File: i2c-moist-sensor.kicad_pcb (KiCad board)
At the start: 2 copper layers, 18 x 149 mm, 24 parts, among them IC1 ATTINY441-SSU, P1 CONN_02X03, X1 16MHz

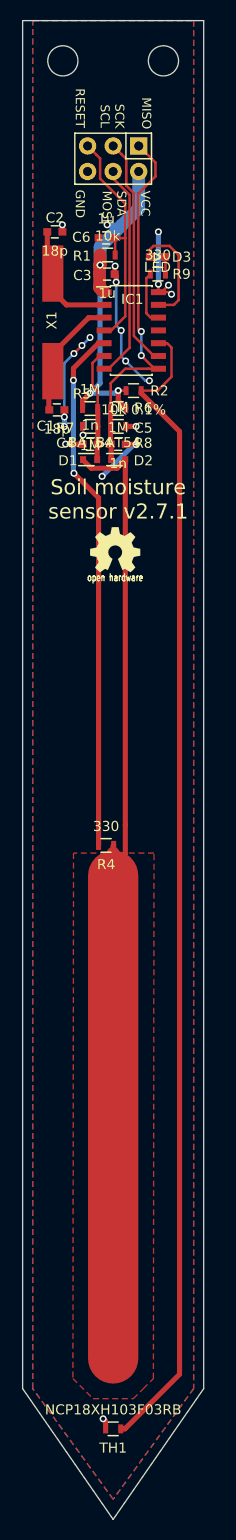
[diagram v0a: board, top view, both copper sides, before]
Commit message: New eeschema libs are new. Move TH1 and R4 OUT of the soil. Minimize stray capacitance where it matters
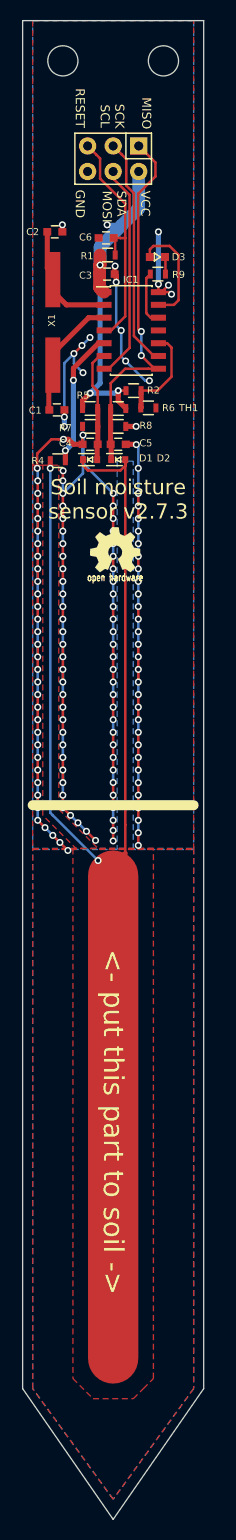
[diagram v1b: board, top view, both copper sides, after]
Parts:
- added G***: LOGO, chirp_logo:ziogas, F.Cu at (95.5, 37.0)
- moved TH1 101.6 mm to (98.5, 51.5), turned to 0 degrees
- moved R4 38.5 mm to (89.5, 56.8), turned to 0 degrees
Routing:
- net GND: track 43.6 -> 223.7 mm, vias 21 -> 144
- net /THERMISTOR: track 115.4 -> 9.70 mm
- net /SENSOR_TRACK: track 98.7 -> 140.8 mm, vias 0 -> 2
- net /EXCITATION: track 52.6 -> 13.6 mm
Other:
- net class excitation added: clearance 0.6, trace_width 0.254, via_dia 0.7, via_drill 0.4
- board text added: "<- put this part to soil ->"
- board text added: "Soil moisture sensor v2.7.3"
- board text removed: "Soil moisture sensor v2.7.1"

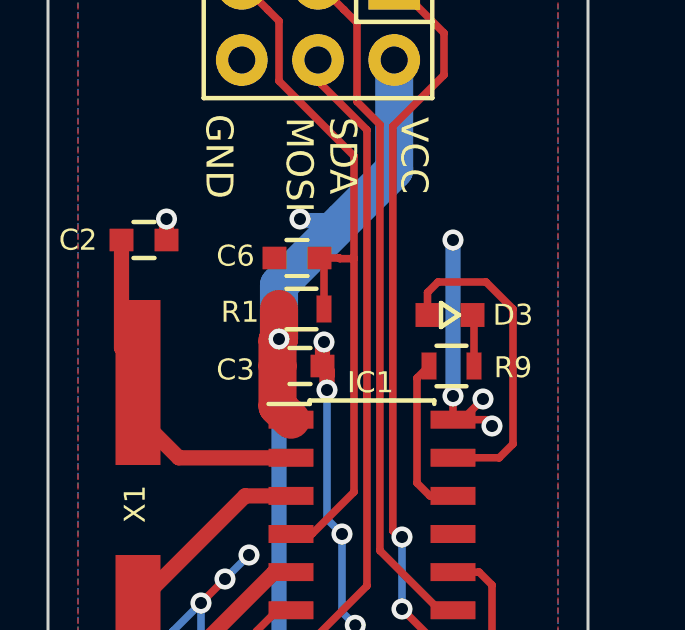
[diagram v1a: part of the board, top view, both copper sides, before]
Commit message: Fix LED footprint according to the datasheet, add data for the bom to schematics
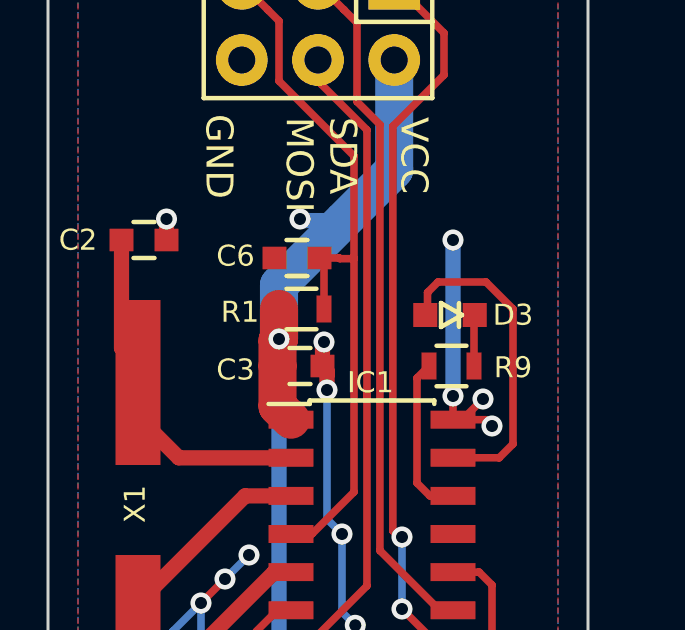
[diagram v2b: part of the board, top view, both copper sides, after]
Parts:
- turned D3 to 270 degrees
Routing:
- net Net-(D3-Pad2): track 1.72 -> 4.57 mm
- net Net-(D3-Pad1): track 10.8 -> 7.96 mm
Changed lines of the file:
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@@
-(kicad_pcb (version 4) (host pcbnew 0.201510221816+6274~30~ubuntu14.04.1-product)
+(kicad_pcb (version 4) (host pcbnew 0.201510241816+6277~30~ubuntu14.04.1-product)
   (general
     (links 42)
-    (no_connects 0)
-    (area 85.949999 12.949999 104.050001 162.050001)
+    (no_connects 2)
+    (area 83.111667 11.7445 114.755001 162.050001)
     (thickness 1.6)
     (drawings 16)
@@
     (pad_drill 0)
     (pad_to_mask_clearance 0)
+    (pad_to_paste_clearance -0.003)
     (aux_axis_origin 0 0)
-    (visible_elements FFFEFF7F)
+    (visible_elements FFFFFF7F)
     (pcbplotparams
       (layerselection 0x010f0_80000001)
@@
     (uvia_drill 0.127)
   )
+  (module LEDs:LED-0603 (layer F.Cu)
+    (at 99.4 36.5 270)
+    (descr "LED 0603 smd package")
+    (tags "LED led 0603 SMD smd SMT smt smdled SMDLED smtled SMTLED")
+    (attr smd)
+    (fp_text reference D3 (at 0 -2.1 360) (layer F.SilkS)
+      (effects (font (size 0.7 0.7) (thickness 0.11)))
+    )
+    (fp_text value LED (at 0 -4.1 360) (layer F.Fab)
+      (effects (font (size 0.7 0.7) (thickness 0.11)))
+    )
+    (fp_line (start 0.4 -0.3) (end -0.4 -0.3) (layer F.SilkS) (width 0.15))
+    (fp_line (start 0.4 0.3) (end 0 -0.4) (layer F.SilkS) (width 0.15))
+    (fp_line (start -0.4 0.3) (end 0.4 0.3) (layer F.SilkS) (width 0.15))
+    (fp_line (start 0 -0.4) (end -0.4 0.3) (layer F.SilkS) (width 0.15))
+    (pad 1 smd rect (at 0 0.825 270) (size 0.8 0.8) (layers F.Cu F.Paste F.Mask)
+      (net 11 "Net-(D3-Pad1)"))
+    (pad 2 smd rect (at 0 -0.825 270) (size 0.8 0.8) (layers F.Cu F.Paste F.Mask)
+      (net 10 "Net-(D3-Pad2)"))
+  )
   (module Crystals:Crystal_HC49-SD_SMD (layer F.Cu)
     (at 89 43 90)
@@
     (pad 2 smd rect (at 0.7 0 180) (size 0.6 0.7) (layers F.Cu F.Paste F.Mask)
       (net 6 /SENSOR_TRACK))
-  )
-  (module LEDs:LED-0603 (layer F.Cu)
-    (at 99.4 36.5)
-    (descr "LED 0603 smd package")
-    (tags "LED led 0603 SMD smd SMT smt smdled SMDLED smtled SMTLED")
-    (attr smd)
-    (fp_text reference D3 (at 2.1 0) (layer F.SilkS)
-      (effects (font (size 0.7 0.7) (thickness 0.11)))
-    )
-    (fp_text value LED (at 4.1 0) (layer F.Fab)
-      (effects (font (size 0.7 0.7) (thickness 0.11)))
-    )
-    (fp_line (start -0.3 -0.4) (end -0.3 0.4) (layer F.SilkS) (width 0.15))
-    (fp_line (start -0.3 0.4) (end 0.3 0) (layer F.SilkS) (width 0.15))
-    (fp_line (start 0.3 0) (end -0.3 -0.4) (layer F.SilkS) (width 0.15))
-    (pad 1 smd rect (at -0.7493 0) (size 0.79756 0.79756) (layers F.Cu F.Paste F.Mask)
-      (net 11 "Net-(D3-Pad1)"))
-    (pad 2 smd rect (at 0.7493 0) (size 0.79756 0.79756) (layers F.Cu F.Paste F.Mask)
-      (net 10 "Net-(D3-Pad2)"))
   )
   (module Pin_Headers:Pin_Header_Straight_2x03 (layer F.Cu)
@@
   (segment (start 100.2 38.2) (end 100.2 36.5507) (width 0.254) (layer F.Cu) (net 10))
   (segment (start 100.2 36.5507) (end 100.1493 36.5) (width 0.254) (layer F.Cu) (net 10))
+  (segment (start 100.6 35.4) (end 99 35.4) (width 0.254) (layer F.Cu) (net 10))
+  (segment (start 99 35.4) (end 98.6507 35.7493) (width 0.254) (layer F.Cu) (net 10))
+  (segment (start 98.6507 35.7493) (end 98.6507 36.5) (width 0.254) (layer F.Cu) (net 10))
   (segment (start 99.5 41.26) (end 101.04 41.26) (width 0.254) (layer F.Cu) (net 11))
   (segment (start 101.04 41.26) (end 101.5 40.8) (width 0.254) (layer F.Cu) (net 11))
   (segment (start 101.5 40.8) (end 101.5 36.3) (width 0.254) (layer F.Cu) (net 11))
   (segment (start 101.5 36.3) (end 100.6 35.4) (width 0.254) (layer F.Cu) (net 11))
-  (segment (start 100.6 35.4) (end 99 35.4) (width 0.254) (layer F.Cu) (net 11))
-  (segment (start 99 35.4) (end 98.6507 35.7493) (width 0.254) (layer F.Cu) (net 11))
-  (segment (start 98.6507 35.7493) (end 98.6507 36.5) (width 0.254) (layer F.Cu) (net 11))
   (segment (start 96.3 29.38933) (end 96.3 26.76) (width 0.254) (layer F.Cu) (net 12))
   (segment (start 97.06362 30.152949) (end 96.3 29.38933) (width 0.254) (layer F.Cu) (net 12))

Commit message: Put the new version to the pannel
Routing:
- net Net-(D3-Pad2): track 4.57 -> 1.72 mm
- net Net-(D3-Pad1): track 7.96 -> 10.8 mm
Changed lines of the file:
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@@
-(kicad_pcb (version 4) (host pcbnew 0.201510241816+6277~30~ubuntu14.04.1-product)
+(kicad_pcb (version 4) (host pcbnew 0.201510251816+6278~30~ubuntu14.04.1-product)
   (general
     (links 42)
-    (no_connects 2)
-    (area 83.111667 11.7445 114.755001 162.050001)
+    (no_connects 0)
+    (area 85.949999 12.949999 104.050001 162.050001)
     (thickness 1.6)
     (drawings 16)
@@
     (visible_elements FFFFFF7F)
     (pcbplotparams
-      (layerselection 0x010f0_80000001)
+      (layerselection 0x010f8_80000001)
       (usegerberextensions false)
       (excludeedgelayer true)
@@
       (effects (font (size 0.7 0.7) (thickness 0.11)))
     )
-    (fp_text value BAT54 (at -5.996 0.142 180) (layer F.Fab)
+    (fp_text value BAT54 (at -7.246 0.142 180) (layer F.Fab)
       (effects (font (size 0.7 0.7) (thickness 0.11)))
     )
@@
       (effects (font (size 0.7 0.7) (thickness 0.11)))
     )
-    (fp_text value BAT54 (at -12.54 0.142 180) (layer F.Fab)
+    (fp_text value BAT54 (at -13.54 0.142 180) (layer F.Fab)
       (effects (font (size 0.7 0.7) (thickness 0.11)))
     )
@@
   (segment (start 100.2 38.2) (end 100.2 36.5507) (width 0.254) (layer F.Cu) (net 10))
   (segment (start 100.2 36.5507) (end 100.1493 36.5) (width 0.254) (layer F.Cu) (net 10))
-  (segment (start 100.6 35.4) (end 99 35.4) (width 0.254) (layer F.Cu) (net 10))
-  (segment (start 99 35.4) (end 98.6507 35.7493) (width 0.254) (layer F.Cu) (net 10))
-  (segment (start 98.6507 35.7493) (end 98.6507 36.5) (width 0.254) (layer F.Cu) (net 10))
+  (segment (start 100.6 35.4) (end 99 35.4) (width 0.254) (layer F.Cu) (net 11))
+  (segment (start 99 35.4) (end 98.6507 35.7493) (width 0.254) (layer F.Cu) (net 11))
+  (segment (start 98.6507 35.7493) (end 98.6507 36.5) (width 0.254) (layer F.Cu) (net 11))
   (segment (start 99.5 41.26) (end 101.04 41.26) (width 0.254) (layer F.Cu) (net 11))
   (segment (start 101.04 41.26) (end 101.5 40.8) (width 0.254) (layer F.Cu) (net 11))

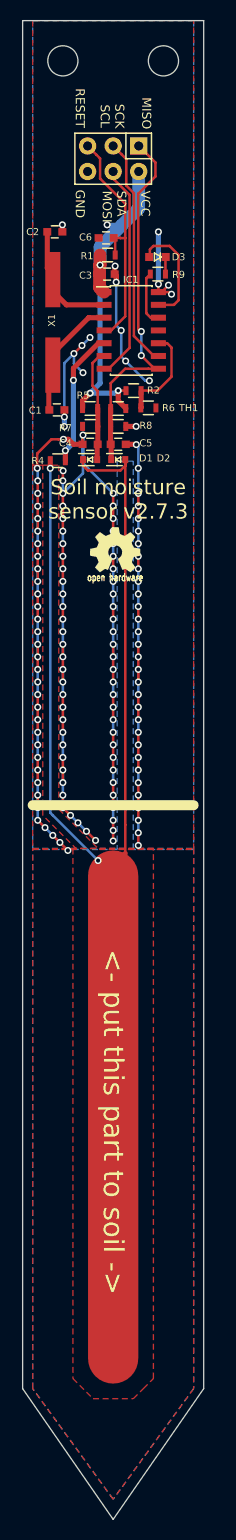
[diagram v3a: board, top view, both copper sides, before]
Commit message: Remove sharp corners so that heatshrink lays nicer
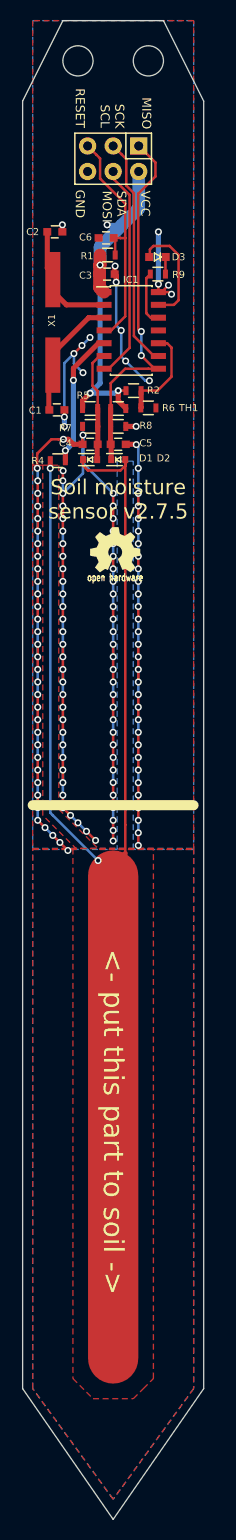
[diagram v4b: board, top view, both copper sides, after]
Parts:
- moved REF** 1.50 mm to (91.5, 17.0)
- moved REF** 1.50 mm to (98.5, 17.0)
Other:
- outline, holes or cut-outs redrawn
- board text added: "Soil moisture sensor v2.7.5"
- board text removed: "Soil moisture sensor v2.7.3"
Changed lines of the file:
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@@
-(kicad_pcb (version 4) (host pcbnew 0.201510251816+6278~30~ubuntu14.04.1-product)
+(kicad_pcb (version 20160815) (host pcbnew no-vcs-found-7518~57~ubuntu14.04.1)
   (general
     (links 42)
@@
     (area 85.949999 12.949999 104.050001 162.050001)
     (thickness 1.6)
-    (drawings 16)
+    (drawings 20)
     (tracks 462)
     (zones 0)
@@
       (hpglpenspeed 20)
       (hpglpendiameter 15)
-      (hpglpenoverlay 2)
       (psnegative false)
       (psa4output false)
@@
     (tags "LED led 0603 SMD smd SMT smt smdled SMDLED smtled SMTLED")
     (attr smd)
-    (fp_text reference D3 (at 0 -2.1 360) (layer F.SilkS)
-      (effects (font (size 0.7 0.7) (thickness 0.11)))
-    )
-    (fp_text value LED (at 0 -4.1 360) (layer F.Fab)
+    (fp_text reference D3 (at 0 -2.1) (layer F.SilkS)
+      (effects (font (size 0.7 0.7) (thickness 0.11)))
+    )
+    (fp_text value LED (at 0 -4.1) (layer F.Fab)
       (effects (font (size 0.7 0.7) (thickness 0.11)))
     )
@@
     (pad 2 smd rect (at 0 -0.825 270) (size 0.8 0.8) (layers F.Cu F.Paste F.Mask)
       (net 10 "Net-(D3-Pad2)"))
+    (model "${KIPRJMOD}/3d/User Library-LTST-C190GKT.STEP"
+      (at (xyz 0 0 0))
+      (scale (xyz 1 1 1))
+      (rotate (xyz 0 0 0))
+    )
   )
   (module Crystals:Crystal_HC49-SD_SMD (layer F.Cu)
@@
     (pad 2 smd rect (at 4.25 0 90) (size 5.5 1.5) (layers F.Cu F.Paste F.Mask)
       (net 3 "Net-(C2-Pad1)"))
-    (model Crystals_Oscillators_SMD/Q_49U3HMS.wrl
+    (model "${KIPRJMOD}/3d/User Library-Crystal HC49_US-SM.STEP"
       (at (xyz 0 0 0))
       (scale (xyz 1 1 1))
@@
     (pad 2 smd rect (at 0.7 0 180) (size 0.6 0.7) (layers F.Cu F.Paste F.Mask)
       (net 14 /MISO/SENSE_HIGH))
+    (model "${KIPRJMOD}/3d/User Library-SOD523-2.STEP"
+      (at (xyz 0 0 0))
+      (scale (xyz 1 1 1))
+      (rotate (xyz -90 0 90))
+    )
   )
   (module SMD_Packages:SOD-523 (layer F.Cu)
@@
     (pad 2 smd rect (at 0.7 0 180) (size 0.6 0.7) (layers F.Cu F.Paste F.Mask)
       (net 6 /SENSOR_TRACK))
+    (model "${KIPRJMOD}/3d/User Library-SOD523-2.STEP"
+      (at (xyz 0 0 0))
+      (scale (xyz 1 1 1))
+      (rotate (xyz -90 0 90))
+    )
   )
   (module Pin_Headers:Pin_Header_Straight_2x03 (layer F.Cu)
@@
     (pad 2 smd rect (at 0.75 0) (size 0.8 0.75) (layers F.Cu F.Paste F.Mask)
       (net 2 GND))
-    (model Capacitors_SMD/C_0603.wrl
+    (model "${KIPRJMOD}/3d/User Library-CAP_SMD-1.STEP"
       (at (xyz 0 0 0))
       (scale (xyz 1 1 1))
@@
     (pad 2 smd rect (at 0.75 0) (size 0.8 0.75) (layers F.Cu F.Paste F.Mask)
       (net 2 GND))
-    (model Capacitors_SMD/C_0603.wrl
+    (model "${KIPRJMOD}/3d/User Library-CAP_SMD-1.STEP"
       (at (xyz 0 0 0))
       (scale (xyz 1 1 1))
@@
     (pad 2 smd rect (at 0.75 0) (size 0.8 0.75) (layers F.Cu F.Paste F.Mask)
       (net 2 GND))
-    (model Capacitors_SMD/C_0603.wrl
+    (model "${KIPRJMOD}/3d/User Library-CAP_SMD-1.STEP"
       (at (xyz 0 0 0))
       (scale (xyz 1 1 1))
@@
     (pad 2 smd rect (at 0.75 0 180) (size 0.8 0.75) (layers F.Cu F.Paste F.Mask)
       (net 2 GND))
-    (model Capacitors_SMD/C_0603.wrl
+    (model "${KIPRJMOD}/3d/User Library-CAP_SMD-1.STEP"
       (at (xyz 0 0 0))
       (scale (xyz 1 1 1))
@@
     (pad 2 smd rect (at 0.75 0) (size 0.8 0.75) (layers F.Cu F.Paste F.Mask)
       (net 2 GND))
-    (model Capacitors_SMD/C_0603.wrl
+    (model "${KIPRJMOD}/3d/User Library-CAP_SMD-1.STEP"
       (at (xyz 0 0 0))
       (scale (xyz 1 1 1))
@@
     (pad 2 smd rect (at 0.75 0 180) (size 0.8 0.75) (layers F.Cu F.Paste F.Mask)
       (net 2 GND))
-    (model Capacitors_SMD/C_0603.wrl
+    (model "${KIPRJMOD}/3d/User Library-CAP_SMD-1.STEP"
       (at (xyz 0 0 0))
       (scale (xyz 1 1 1))
@@
     (pad 2 smd rect (at 0.75 0 180) (size 0.5 0.9) (layers F.Cu F.Paste F.Mask)
       (net 4 VCC))
-    (model Resistors_SMD/R_0603.wrl
+    (model "${KIPRJMOD}/3d/User Library-RES_SMD-1.STEP"
       (at (xyz 0 0 0))
       (scale (xyz 1 1 1))
@@
     (pad 2 smd rect (at 0.75 0) (size 0.5 0.9) (layers F.Cu F.Paste F.Mask)
       (net 7 /THERMISTOR))
-    (model Resistors_SMD/R_0603.wrl
+    (model "${KIPRJMOD}/3d/User Library-RES_SMD-1.STEP"
       (at (xyz 0 0 0))
       (scale (xyz 1 1 1))
@@
     (pad 2 smd rect (at 0.75 0) (size 0.5 0.9) (layers F.Cu F.Paste F.Mask)
       (net 9 /EXCITATION))
-    (model Resistors_SMD/R_0603.wrl
+    (model "${KIPRJMOD}/3d/User Library-RES_SMD-1.STEP"
       (at (xyz 0 0 0))
       (scale (xyz 1 1 1))
@@
     (pad 2 smd rect (at 0.75 0 180) (size 0.5 0.9) (layers F.Cu F.Paste F.Mask)
       (net 4 VCC))
-    (model Resistors_SMD/R_0603.wrl
+    (model "${KIPRJMOD}/3d/User Library-RES_SMD-1.STEP"
       (at (xyz 0 0 0))
       (scale (xyz 1 1 1))
@@
     (pad 2 smd rect (at 0.75 0) (size 0.5 0.9) (layers F.Cu F.Paste F.Mask)
       (net 4 VCC))
-    (model Resistors_SMD/R_0603.wrl
+    (model "${KIPRJMOD}/3d/User Library-RES_SMD-1.STEP"
       (at (xyz 0 0 0))
       (scale (xyz 1 1 1))
@@
     (pad 2 smd rect (at 0.75 0) (size 0.5 0.9) (layers F.Cu F.Paste F.Mask)
       (net 5 /SENSE_LOW))
-    (model Resistors_SMD/R_0603.wrl
+    (model "${KIPRJMOD}/3d/User Library-RES_SMD-1.STEP"
       (at (xyz 0 0 0))
       (scale (xyz 1 1 1))
@@
     (pad 2 smd rect (at 0.75 0 180) (size 0.5 0.9) (layers F.Cu F.Paste F.Mask)
       (net 14 /MISO/SENSE_HIGH))
-    (model Resistors_SMD/R_0603.wrl
+    (model "${KIPRJMOD}/3d/User Library-RES_SMD-1.STEP"
       (at (xyz 0 0 0))
       (scale (xyz 1 1 1))
@@
     (pad 2 smd rect (at 0.75 0 180) (size 0.5 0.9) (layers F.Cu F.Paste F.Mask)
       (net 16 "Net-(IC1-Pad12)"))
-    (model Resistors_SMD/R_0603.wrl
+    (model "${KIPRJMOD}/3d/User Library-RES_SMD-1.STEP"
       (at (xyz 0 0 0))
       (scale (xyz 1 1 1))
@@
     (pad 2 smd rect (at 0.75 0) (size 0.5 0.9) (layers F.Cu F.Paste F.Mask)
       (net 2 GND))
-    (model Resistors_SMD/R_0603.wrl
+    (model "${KIPRJMOD}/3d/User Library-RES_SMD-1.STEP"
       (at (xyz 0 0 0))
       (scale (xyz 1 1 1))
@@
   )
   (module Mounting_Holes:MountingHole_3mm (layer F.Cu)
-    (at 90 17)
+    (at 91.5 17)
     (descr "Mounting hole, Befestigungsbohrung, 3mm, No Annular, Kein Restring,")
     (tags "Mounting hole, Befestigungsbohrung, 3mm, No Annular, Kein Restring,")
@@
   )
   (module Mounting_Holes:MountingHole_3mm (layer F.Cu)
-    (at 100 17)
+    (at 98.5 17)
     (descr "Mounting hole, Befestigungsbohrung, 3mm, No Annular, Kein Restring,")
     (tags "Mounting hole, Befestigungsbohrung, 3mm, No Annular, Kein Restring,")
@@
     (pad 14 smd rect (at 2.7 -3.81) (size 1.5 0.6) (layers F.Cu F.Paste F.Mask)
       (net 2 GND))
-    (model Housings_SOIC.3dshapes/SOIC-14_3.9x8.7mm_Pitch1.27mm.wrl
-      (at (xyz 0 0 0))
-      (scale (xyz 1 1 1))
-      (rotate (xyz 0 0 0))
+    (model "${KIPRJMOD}/3d/User Library-SOIC-14.STEP"
+      (at (xyz 0 0 0))
+      (scale (xyz 1 1 1))
+      (rotate (xyz 0 0 90))
     )
   )
@@
       (xy 18.376834 -6.315505) (xy 18.387358 -6.35) (xy 18.451288 -6.557312) (xy 18.477643 -6.43786)) (layer B.SilkS) (width 0.01))
   )
+  (dimension 18 (width 0.175) (layer Cmts.User)
+    (gr_text "18,000 mm" (at 95 162.7) (layer Cmts.User)
+      (effects (font (size 0.7 0.7) (thickness 0.175)))
+    )
+    (feature1 (pts (xy 104 149) (xy 104 163.4)))
+    (feature2 (pts (xy 86 149) (xy 86 163.4)))
+    (crossbar (pts (xy 86 162) (xy 104 162)))
+    (arrow1a (pts (xy 104 162) (xy 102.873496 162.586421)))
+    (arrow1b (pts (xy 104 162) (xy 102.873496 161.413579)))
+    (arrow2a (pts (xy 86 162) (xy 87.126504 162.586421)))
+    (arrow2b (pts (xy 86 162) (xy 87.126504 161.413579)))
+  )
+  (dimension 149 (width 0.175) (layer Cmts.User)
+    (gr_text "149,000 mm" (at 108.95 87.5 270) (layer Cmts.User)
+      (effects (font (size 0.7 0.7) (thickness 0.175)))
+    )
+    (feature1 (pts (xy 104 162) (xy 109.65 162)))
+    (feature2 (pts (xy 104 13) (xy 109.65 13)))
+    (crossbar (pts (xy 108.25 13) (xy 108.25 162)))
+    (arrow1a (pts (xy 108.25 162) (xy 107.663579 160.873496)))
+    (arrow1b (pts (xy 108.25 162) (xy 108.836421 160.873496)))
+    (arrow2a (pts (xy 108.25 13) (xy 107.663579 14.126504)))
+    (arrow2b (pts (xy 108.25 13) (xy 108.836421 14.126504)))
+  )
+  (gr_line (start 86 21) (end 90 13) (layer Edge.Cuts) (width 0.1))
+  (gr_line (start 104 21) (end 100 13) (layer Edge.Cuts) (width 0.1))
   (gr_text "Catnip Electronics\nhttp://wemakethings.net/chirp\nmic@wemakethings.net" (at 97 72 270) (layer B.SilkS)
     (effects (font (size 1.5 1.5) (thickness 0.3)) (justify mirror))
@@
     (effects (font (size 0.9 0.9) (thickness 0.2)) (justify right))
   )
-  (gr_text "Soil moisture \nsensor v2.7.3" (at 95.5 60.6) (layer F.SilkS)
+  (gr_text "Soil moisture \nsensor v2.7.5" (at 95.5 60.6) (layer F.SilkS)
     (effects (font (size 1.5 1.5) (thickness 0.3)))
   )
   (gr_line (start 95 162) (end 86 149) (angle 90) (layer Edge.Cuts) (width 0.1))
   (gr_line (start 95 162) (end 104 149) (angle 90) (layer Edge.Cuts) (width 0.1))
-  (gr_line (start 86 13) (end 86 149) (angle 90) (layer Edge.Cuts) (width 0.1))
-  (gr_line (start 104 13) (end 86 13) (angle 90) (layer Edge.Cuts) (width 0.1))
-  (gr_line (start 104 149) (end 104 13) (angle 90) (layer Edge.Cuts) (width 0.1))
+  (gr_line (start 86 21) (end 86 149) (angle 90) (layer Edge.Cuts) (width 0.1))
+  (gr_line (start 100 13) (end 90 13) (angle 90) (layer Edge.Cuts) (width 0.1))
+  (gr_line (start 104 149) (end 104 21) (angle 90) (layer Edge.Cuts) (width 0.1))
   (segment (start 94.1 42.53) (end 92.5688 42.53) (width 0.508) (layer F.Cu) (net 1))
   (segment (start 92.5688 42.53) (end 89 46.0988) (width 0.508) (layer F.Cu) (net 1))
@@
       (pts
         (xy 103 149) (xy 95 160) (xy 87 149) (xy 87 95.3) (xy 103 95.3)
-        (xy 103 149)
       )
     )
@@
       (pts
         (xy 103 149) (xy 95 160) (xy 87 149) (xy 87 95.3) (xy 103 95.3)
-        (xy 103 149)
       )
     )
